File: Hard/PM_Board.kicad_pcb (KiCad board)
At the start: 2 copper layers, 70 x 60 mm, 69 parts, among them J1 Micro_SD_Card_Det_Hirose_DM3AT, J101 LiPo_V+, J102 LiPo_V-, J2 KRC_Conn_SWD, J3 USB_B_Micro, J4 KRC_Conn_CAN, J5 KRC_Conn_CAN, J6 KRC_Conn_CAN, Q1 RSS100N03, U1 CY8C58xxLTI-LPxxx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

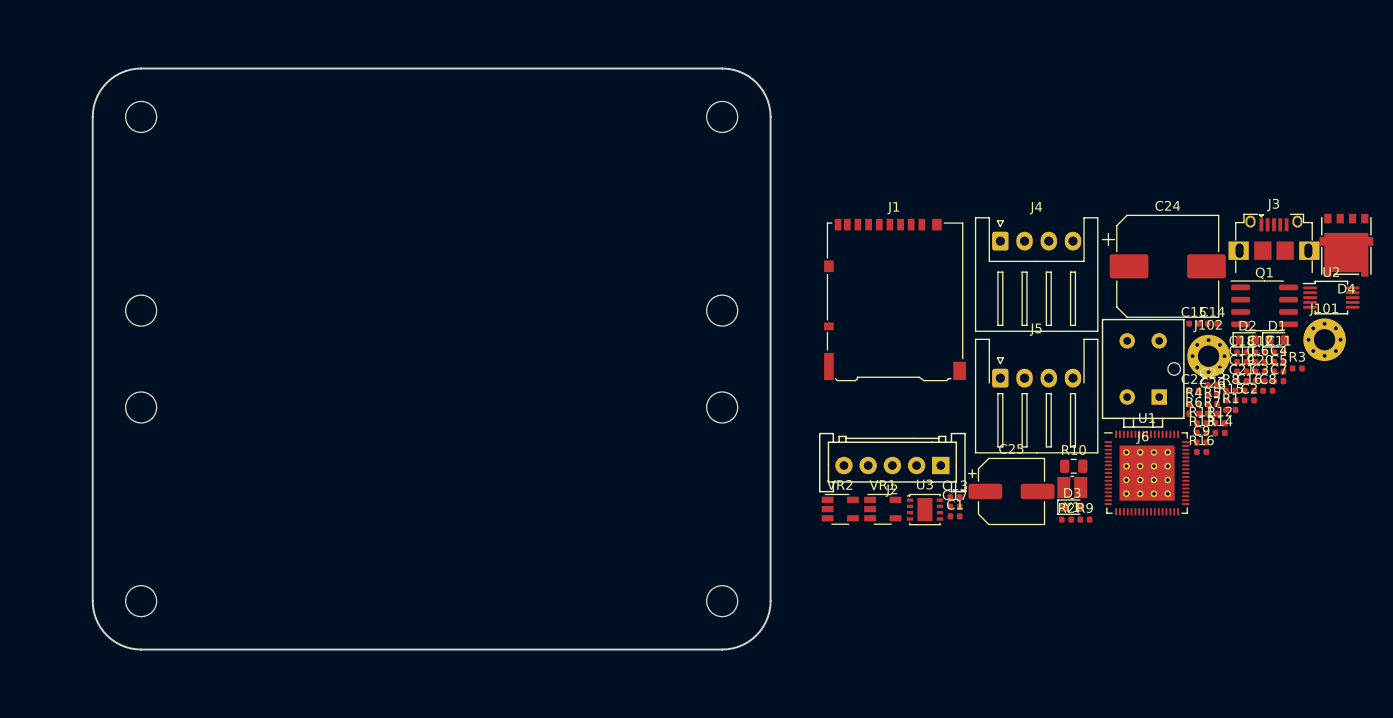
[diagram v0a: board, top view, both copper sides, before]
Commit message: [add] 部品配置仮完了
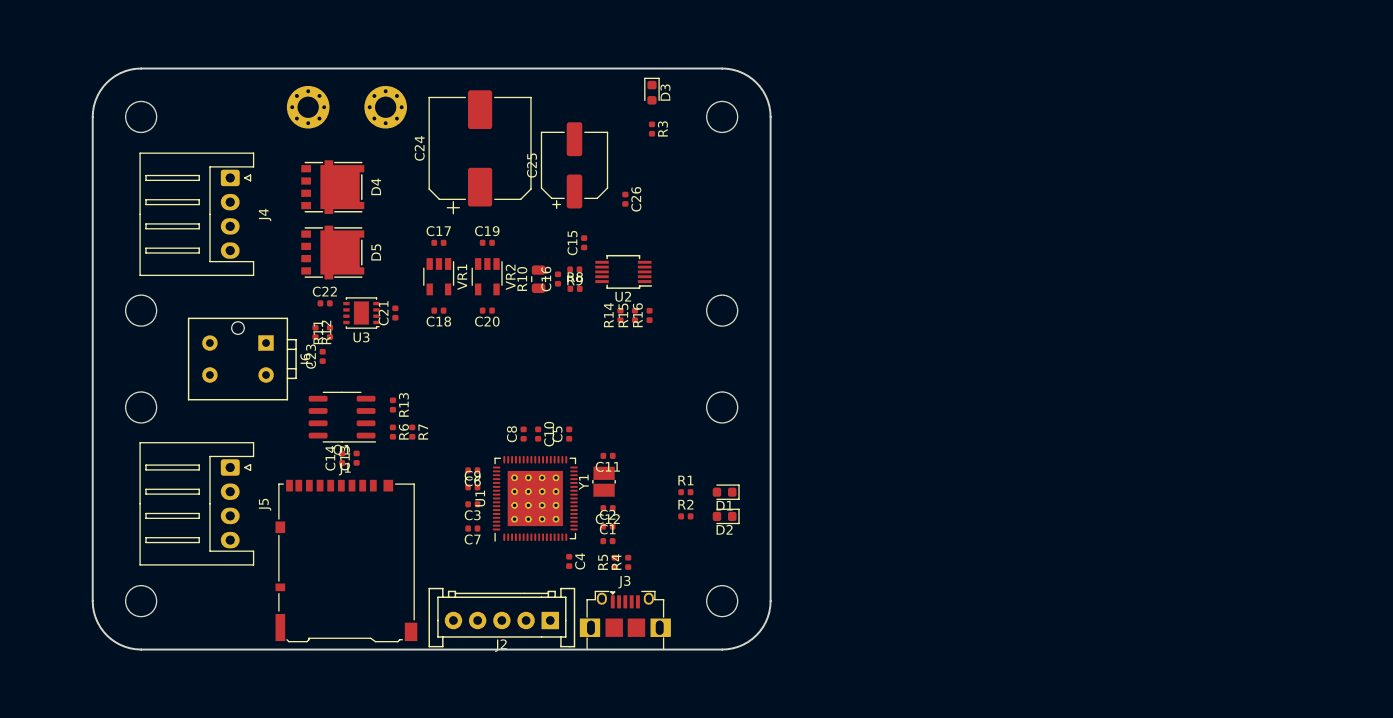
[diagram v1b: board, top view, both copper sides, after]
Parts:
- added D5: NTS1545, KUTKiCad_footprint:DFN5_5x6_1.27P, F.Cu at (145.5, 94.0)
- J5: footprint Connector_JST:JST_XH_S4B-XH-A-1_1x04_P2.50mm_Horizontal -> Connector_JST:JST_XH_S4B-XH-A_1x04_P2.50mm_Horizontal
- moved J101 107.7 mm to (142.2, 79.0)
- moved D4 104.2 mm to (145.5, 87.2), turned to 90 degrees
- moved Q1 95.9 mm to (145.8, 111.0), turned to 180 degrees
- moved R12 93.9 mm to (143.0, 102.2), turned to 270 degrees
- moved J6 93.5 mm to (135.0, 105.0), turned to 90 degrees
- moved C23 91.9 mm to (143.8, 104.7), turned to 90 degrees
- moved C14 90.9 mm to (145.8, 115.2), turned to 90 degrees
- moved R11 90.5 mm to (144.5, 102.2), turned to 90 degrees
- moved C22 90.2 mm to (144.0, 99.2)
- moved J102 88.8 mm to (150.2, 79.0)
- moved C21 87.7 mm to (151.2, 100.2), turned to 90 degrees
- moved C7 84.6 mm to (159.2, 122.5), turned to 180 degrees
- moved R13 83.6 mm to (151.0, 109.8), turned to 270 degrees
- moved C18 83.0 mm to (155.8, 100.0), turned to 180 degrees
- moved R6 82.7 mm to (151.0, 112.5), turned to 270 degrees
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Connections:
- J6 pad 2: VCC -> Net-(D5-Pad2)
- Q1 pad 1: /Power_Cutoff -> GND
- Q1 pad 3: Net-(J4-Pad1) -> GND
- Q1 pad 4: (no net) -> /Power_Cutoff
- Q1 pad 5: (no net) -> Net-(J4-Pad1)
- Q1 pad 6: (no net) -> Net-(J4-Pad1)
- Q1 pad 7: (no net) -> Net-(J4-Pad1)
- Q1 pad 8: (no net) -> Net-(J4-Pad1)
- R16 pad 2: /INA226_Aleart -> /INA226_Alert
- U1 pad 21: /INA226_Aleart -> /INA226_Alert
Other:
- net class Default: clearance 0.2 -> 0.18; via_dia 0.8 -> 0.6; via_drill 0.4 -> 0.3
- rule trace_clearance: 0.2 -> 0.18

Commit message: [add] 配線中だよ
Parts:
- added Q2: 2n7002, Package_TO_SOT_SMD:SOT-23, F.Cu at (138.4, 107.4)
- added R17: 10k, Resistor_SMD:R_0402_1005Metric, F.Cu at (148.0, 107.8)
- Q1: value RSS100N03 -> SSM6J501NU; footprint Package_SO:SOIC-8_3.9x4.9mm_P1.27mm -> KUTKiCad_footprint:UDFN6B
- R14: value 10k -> 1k
- moved D3 56.0 mm to (170.0, 133.0), turned to 90 degrees
- moved R3 49.4 mm to (170.0, 130.0), turned to 90 degrees
- moved U2 39.5 mm to (135.5, 100.2), turned to 0 degrees
- moved C15 38.7 mm to (133.3, 102.8), turned to 180 degrees
- moved R14 35.9 mm to (139.9, 110.0), turned to 0 degrees
- moved R15 32.3 mm to (144.5, 107.8), turned to 270 degrees
- moved R16 32.1 mm to (146.2, 107.8), turned to 270 degrees
- moved R11 30.5 mm to (134.9, 131.2), turned to 0 degrees
- moved R9 29.2 mm to (141.0, 100.6)
- moved R8 28.8 mm to (141.0, 98.4), turned to 180 degrees
- moved C16 28.7 mm to (139.5, 99.5), turned to 270 degrees
- moved R12 28.6 mm to (134.9, 129.7), turned to 180 degrees
- moved C23 28.1 mm to (132.5, 130.4), turned to 0 degrees
- moved J1 27.2 mm to (172.7, 119.6), turned to 90 degrees
- moved C21 27.0 mm to (143.6, 126.1)
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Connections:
- J4 pad 1: Net-(J4-Pad1) -> GND
- J4 pad 2: Net-(C17-Pad1) -> Net-(J4-Pad2)
- J5 pad 1: Net-(J4-Pad1) -> GND
- J5 pad 2: Net-(C17-Pad1) -> Net-(J4-Pad2)
- Q1 pad 1: GND -> Net-(J4-Pad2)
- Q1 pad 2: GND -> Net-(J4-Pad2)
- Q1 pad 3: GND -> Net-(Q1-Pad3)
- Q1 pad 4: /Power_Cutoff -> Net-(C17-Pad1)
- Q1 pad 5: Net-(J4-Pad1) -> Net-(J4-Pad2)
- Q1 pad 6: Net-(J4-Pad1) -> Net-(J4-Pad2)
- Q1 pad 7: Net-(J4-Pad1) -> Net-(J4-Pad2)
- Q1 pad 8: Net-(J4-Pad1) -> Net-(C17-Pad1)
- R13 pad 1: /Power_Cutoff -> Net-(C17-Pad1)
- R13 pad 2: GND -> Net-(Q1-Pad3)
- R14 pad 1: +3V3 -> /Power_Cutoff
- R14 pad 2: /INA226_SDA -> GND
- R16 pad 2: /INA226_Alert -> /INA226_SDA
- U1 pad 19: /Power_Cutoff -> Net-(U1-Pad19)
- U1 pad 20: /INA226_SCL -> Net-(U1-Pad20)
- U1 pad 21: /INA226_Alert -> Net-(U1-Pad21)
- U1 pad 36: Net-(U1-Pad36) -> /SD_MISO
- U1 pad 37: Net-(U1-Pad37) -> /SD_CLK
- U1 pad 38: Net-(U1-Pad38) -> /SD_MOSI
- U1 pad 39: Net-(U1-Pad39) -> /SD_CS
- U1 pad 4: /INA226_SDA -> Net-(U1-Pad4)
- U1 pad 48: Net-(U1-Pad48) -> /INA226_Alert
- U1 pad 49: Net-(U1-Pad49) -> /INA226_SDA
- U1 pad 50: Net-(U1-Pad50) -> /INA226_SCL
- U1 pad 51: Net-(U1-Pad51) -> /Power_Cutoff
- U1 pad 62: /SD_CS -> Net-(U1-Pad62)
- U1 pad 63: /SD_MOSI -> Net-(U1-Pad63)
- U1 pad 64: /SD_CLK -> Net-(U1-Pad64)
- U1 pad 65: /SD_MISO -> Net-(U1-Pad65)
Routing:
- net +3V3: track 0.00 -> 103.0 mm, vias 0 -> 9
- net VCC: track 0.00 -> 94.2 mm
- net Net-(J4-Pad2): track 0.00 -> 45.5 mm
- net Net-(C17-Pad1): track 0.00 -> 39.7 mm
- net /INA226_Alert: track 0.00 -> 30.1 mm, vias 0 -> 2
- net /INA226_SDA: track 0.00 -> 28.5 mm, vias 0 -> 2
- net /INA226_SCL: track 0.00 -> 27.0 mm, vias 0 -> 2
- net +5V: track 0.00 -> 22.9 mm, vias 0 -> 2
- net GND: track 0.00 -> 18.7 mm, vias 0 -> 13
- net Net-(C9-Pad2): track 0.00 -> 16.6 mm, vias 0 -> 2
- net /Power_Cutoff: track 0.00 -> 13.3 mm
- net Net-(R4-Pad2): track 0.00 -> 8.23 mm, vias 0 -> 2
- net Net-(D5-Pad2): track 0.00 -> 7.92 mm
- net Net-(Q1-Pad3): track 0.00 -> 7.24 mm
- net Net-(D4-Pad2): track 0.00 -> 6.71 mm
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- added copper zone on F.Cu, net Net-(C17-Pad1)
- added copper zone on F.Cu, net Net-(D4-Pad2)
- added copper zone on F.Cu, net Net-(D5-Pad2)
- added copper zone on F.Cu, net Net-(J4-Pad2)
- added copper zone on F.Cu, net VCC

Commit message: [add] 基板完成
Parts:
- removed the REF** at (185.0, 100.0)
- removed the REF** at (125.0, 110.0)
- removed the REF** at (125.0, 100.0)
- removed the REF** at (185.0, 130.0)
- removed the REF** at (125.0, 130.0)
- removed the REF** at (185.0, 80.0)
- removed the REF** at (125.0, 80.0)
- added G***: LOGO, logo:Rask_sq, F.Cu at (177.5, 125.0)
- added G***: LOGO, logo:niwatori, F.Cu at (176.2, 83.8)
- added G***: LOGO, logo:arrows, B.Cu at (156.5, 81.0)
- added REF**: MountingHole_3.2mm_M3, MountingHole:MountingHole_3.2mm_M3, F.Cu at (177.5, 95.0)
- added REF**: MountingHole_3.2mm_M3, MountingHole:MountingHole_3.2mm_M3, F.Cu at (117.5, 115.0)
- added REF**: MountingHole_3.2mm_M3, MountingHole:MountingHole_3.2mm_M3, F.Cu at (117.5, 95.0)
- added REF**: MountingHole_3.2mm_M3, MountingHole:MountingHole_3.2mm_M3, F.Cu at (177.5, 75.0)
- added REF**: MountingHole_3.2mm_M3, MountingHole:MountingHole_3.2mm_M3, F.Cu at (177.5, 135.0)
- added REF**: MountingHole_3.2mm_M3, MountingHole:MountingHole_3.2mm_M3, F.Cu at (117.5, 135.0)
- added REF**: MountingHole_3.2mm_M3, MountingHole:MountingHole_3.2mm_M3, F.Cu at (117.5, 75.0)
- moved D3 31.4 mm to (178.8, 102.9), turned to 180 degrees
- moved D2 30.1 mm to (178.8, 104.9), turned to 180 degrees
- moved D1 29.1 mm to (178.8, 106.9), turned to 180 degrees
- moved R3 27.7 mm to (175.8, 102.9), turned to 180 degrees
- moved R2 26.3 mm to (175.8, 104.9), turned to 0 degrees
- moved R1 25.1 mm to (175.8, 106.9), turned to 0 degrees
- moved R6 23.0 mm to (154.8, 129.5), turned to 0 degrees
- moved R7 20.4 mm to (154.8, 121.8), turned to 0 degrees
- moved C13 19.2 mm to (154.8, 128.0), turned to 0 degrees
- moved C14 17.0 mm to (154.8, 126.5), turned to 0 degrees
- moved R12 10.1 mm to (125.6, 133.4), turned to 270 degrees
- moved Q1 9.01 mm to (124.0, 102.5)
- moved C22 9.01 mm to (131.5, 128.3), turned to 0 degrees
- moved C4 9.01 mm to (147.3, 131.5)
- moved C1 9.01 mm to (152.3, 128.4)
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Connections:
- U1 pad 13: Net-(U1-Pad13) -> /SD_CS
- U1 pad 14: Net-(U1-Pad14) -> /SD_MOSI
- U1 pad 15: Net-(U1-Pad15) -> /SD_CLK
- U1 pad 16: Net-(U1-Pad16) -> /SD_MISO
- U1 pad 2: /CAN_RXD -> /CAN_STB
- U1 pad 29: Net-(R2-Pad1) -> Net-(U1-Pad29)
- U1 pad 30: Net-(R1-Pad1) -> Net-(U1-Pad30)
- U1 pad 36: /SD_MISO -> Net-(R2-Pad1)
- U1 pad 37: /SD_CLK -> Net-(R1-Pad1)
- U1 pad 38: /SD_MOSI -> Net-(U1-Pad38)
- U1 pad 39: /SD_CS -> Net-(U1-Pad39)
- U1 pad 68: /CAN_STB -> /CAN_RXD
- U3 pad 9: (no net) -> GND
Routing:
- net /CAN_L: track 0.00 -> 79.9 mm, vias 0 -> 2
- net /CAN_H: track 0.00 -> 77.2 mm, vias 0 -> 1
- net GND: track 18.7 -> 56.1 mm, vias 13 -> 134
- net Net-(R2-Pad1): track 0.00 -> 37.3 mm, vias 0 -> 2
- net Net-(R1-Pad1): track 0.00 -> 37.0 mm, vias 0 -> 2
- net +3V3: track 103.0 -> 134.8 mm, vias 9 -> 11
- net /SD_CS: track 0.00 -> 24.0 mm, vias 0 -> 2
- net VCC: track 94.2 -> 116.9 mm
- net /SD_MOSI: track 0.00 -> 22.1 mm, vias 0 -> 2
- net /SD_CLK: track 0.00 -> 18.4 mm, vias 0 -> 2
- net /SD_MISO: track 0.00 -> 17.2 mm, vias 0 -> 2
- net Net-(J2-Pad5): track 0.00 -> 15.9 mm, vias 0 -> 1
- net /CAN_STB: track 0.00 -> 14.9 mm, vias 0 -> 2
- net Net-(C17-Pad1): track 39.7 -> 54.4 mm
- net Net-(J2-Pad4): track 0.00 -> 14.0 mm, vias 0 -> 1
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- added copper zone on B.Cu, net GND
- added copper zone on F.Cu, net GND
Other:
- board size 70 x 60 mm -> 70 x 70 mm
- board text added: "CAN-H"
- board text added: "CAN-L"
- board text added: "CAN-RXD 2[5]"
- board text added: "CAN-STB 2[7]"
- board text added: "CAN-TXD 2[6]"
- board text added: "CLK"
- board text added: "CLK 1[4]"
- board text added: "CS 1[2]"
- board text added: "D1:Status LED A 3[7]"
- board text added: "D2:Status LED B 3[6]"
- board text added: "D3:Power LED"
- board text added: "DIO"
- board text added: "Date"
- board text added: "GND"
- board text added: "GS-8 PM Board Rev.1 Designed by T.Niwa 2019.9"
- board text added: "MISO 1[5]"
- board text added: "MOSI 1[3]"
- board text added: "Manufacturer"
- board text added: "NC"
- board text added: "Note"
- board text added: "RES"
- board text added: "Terminator Only"
- board text added: "Umbilical"
- board text added: "V+"
- board text added: "V-"
- board text added: "VCC"
